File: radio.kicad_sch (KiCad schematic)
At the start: 28 parts, among them U301 CC1101RGPR, Y301 27MHz

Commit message: :package: finished version 1.0.0, generated production files
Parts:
- gave numbers to parts that had none: 4
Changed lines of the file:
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@@
 		(on_board yes)
 		(dnp no)
-		(property "Reference" "TP?"
+		(property "Reference" "TP304"
 			(at 116.84 83.82 0)
 			(effects
@@
 			(project "Antares-Transmitter"
 				(path "/7eacce39-bbdf-4759-aeb5-d69ccfcb7b29/9b82dc90-2c5e-4a12-b0c3-9dc0f854a933"
-					(reference "TP?")
+					(reference "TP304")
 					(unit 1)
 				)
@@
 		(on_board yes)
 		(dnp no)
-		(property "Reference" "TP?"
+		(property "Reference" "TP303"
 			(at 110.49 83.82 0)
 			(effects
@@
 			(project "Antares-Transmitter"
 				(path "/7eacce39-bbdf-4759-aeb5-d69ccfcb7b29/9b82dc90-2c5e-4a12-b0c3-9dc0f854a933"
-					(reference "TP?")
+					(reference "TP303")
 					(unit 1)
 				)
@@
 		(on_board yes)
 		(dnp no)
-		(property "Reference" "TP?"
+		(property "Reference" "TP301"
 			(at 97.79 83.82 0)
 			(effects
@@
 			(project "Antares-Transmitter"
 				(path "/7eacce39-bbdf-4759-aeb5-d69ccfcb7b29/9b82dc90-2c5e-4a12-b0c3-9dc0f854a933"
-					(reference "TP?")
+					(reference "TP301")
 					(unit 1)
 				)
@@
 		(on_board yes)
 		(dnp no)
-		(property "Reference" "TP?"
+		(property "Reference" "TP302"
 			(at 104.14 83.82 0)
 			(effects
@@
 			(project "Antares-Transmitter"
 				(path "/7eacce39-bbdf-4759-aeb5-d69ccfcb7b29/9b82dc90-2c5e-4a12-b0c3-9dc0f854a933"
-					(reference "TP?")
-					(unit 1)
-				)
+					(reference "TP302")
+					(unit 1)
+				)

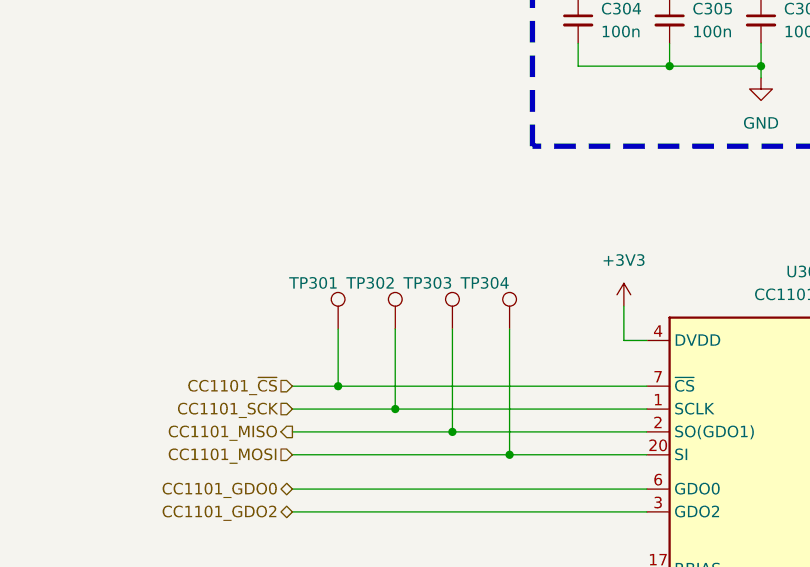
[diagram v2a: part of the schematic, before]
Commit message: :minidisc: fixed some silkscreen, added vias and updated LCSC PNs with Basic components
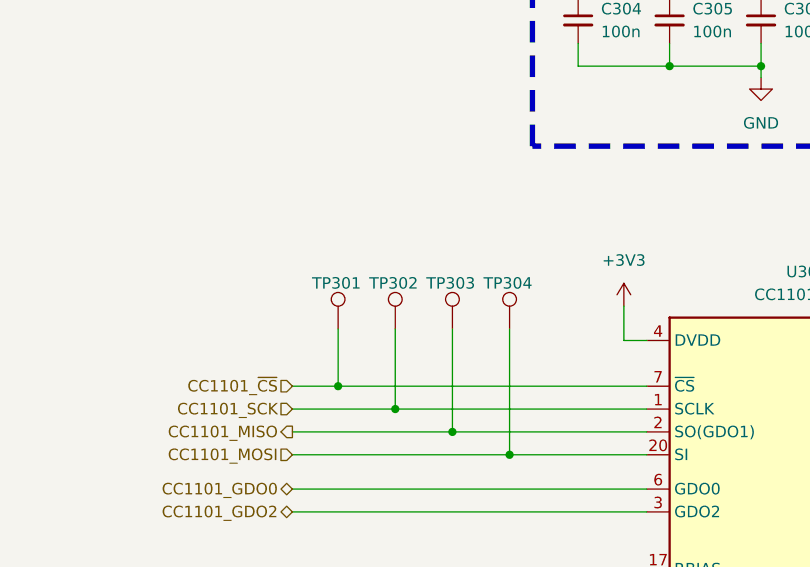
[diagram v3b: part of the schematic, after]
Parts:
- C301, C302: LCSC C107047 -> C1663; PN CC0603JRNPO9BN330 -> CL10C330JB8NNNC
- C309: LCSC C14665 -> C14858; PN CC0603JRNPO9BN101 -> CL10C101JB8NNNC
- C313: LCSC C107034 -> C38523; PN CC0603JRNPO9BN120 -> CL10C120JB8NNNC
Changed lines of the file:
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@@
 		(title "Project Antares - Transmitter Schematic")
 		(date "2024-08-23")
-		(rev "1.0.1")
+		(rev "1.0.2")
 		(company "Ourobors Embedded Development")
 		(comment 1 "Pablo Jean Rozario")
@@
 		(dnp no)
 		(property "Reference" "TP304"
-			(at 116.84 83.82 0)
+			(at 119.38 83.82 0)
 			(effects
 				(font
@@
 		(dnp no)
 		(property "Reference" "TP303"
-			(at 110.49 83.82 0)
+			(at 113.03 83.82 0)
 			(effects
 				(font
@@
 			)
 		)
-		(property "LCSC" "C107047"
+		(property "LCSC" "C1663"
 			(at 83.82 156.21 0)
 			(effects
@@
 			)
 		)
-		(property "PN" "CC0603JRNPO9BN330"
+		(property "PN" "CL10C330JB8NNNC"
 			(at 83.82 156.21 0)
 			(effects
@@
 			)
 		)
-		(property "LCSC" "C14665"
+		(property "LCSC" "C14858"
 			(at 189.23 121.92 0)
 			(effects
@@
 			)
 		)
-		(property "PN" "CC0603JRNPO9BN101"
+		(property "PN" "CL10C101JB8NNNC"
 			(at 189.23 121.92 0)
 			(effects
@@
 		(dnp no)
 		(property "Reference" "TP301"
-			(at 97.79 83.82 0)
+			(at 100.33 83.82 0)
 			(effects
 				(font
@@
 			)
 		)
-		(property "LCSC" "C107034"
+		(property "LCSC" "C38523"
 			(at 251.46 105.41 0)
 			(effects
@@
 			)
 		)
-		(property "PN" "CC0603JRNPO9BN120"
+		(property "PN" "CL10C120JB8NNNC"
 			(at 251.46 105.41 0)
 			(effects
@@
 		(dnp no)
 		(property "Reference" "TP302"
-			(at 104.14 83.82 0)
+			(at 106.68 83.82 0)
 			(effects
 				(font
@@
 			)
 		)
-		(property "LCSC" "C107047"
+		(property "LCSC" "C1663"
 			(at 62.23 156.21 0)
 			(effects
@@
 			)
 		)
-		(property "PN" "CC0603JRNPO9BN330"
+		(property "PN" "CL10C330JB8NNNC"
 			(at 62.23 156.21 0)
 			(effects

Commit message: :memo: added schematic model
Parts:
- C312: LCSC C105622 -> C1671; PN CC0603JRNPO9BN470 -> CL10C470JB8NNNC
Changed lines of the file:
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@@
 			)
 		)
-		(property "LCSC" "C105622"
+		(property "LCSC" "C1671"
 			(at 246.38 109.22 0)
 			(effects
@@
 			)
 		)
-		(property "PN" "CC0603JRNPO9BN470"
+		(property "PN" "CL10C470JB8NNNC"
 			(at 246.38 109.22 0)
 			(effects
